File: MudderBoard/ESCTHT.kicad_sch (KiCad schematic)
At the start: 4 parts, among them U4 LM5122QMH/NOPB

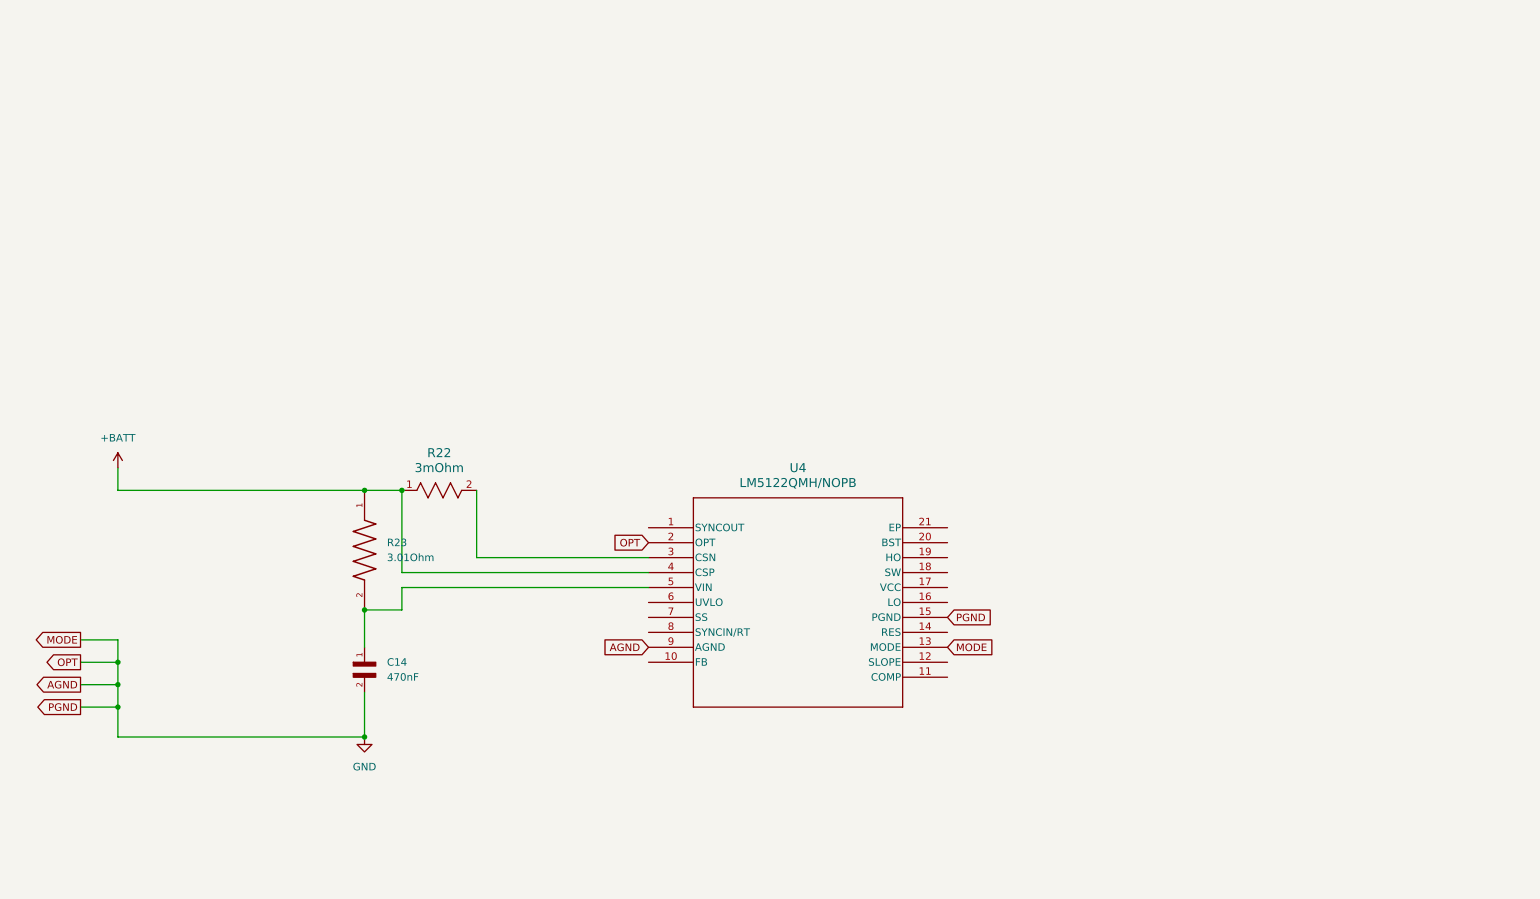
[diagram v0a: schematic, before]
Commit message: Updating the ESC Controller
Completed design without selecting footprints.
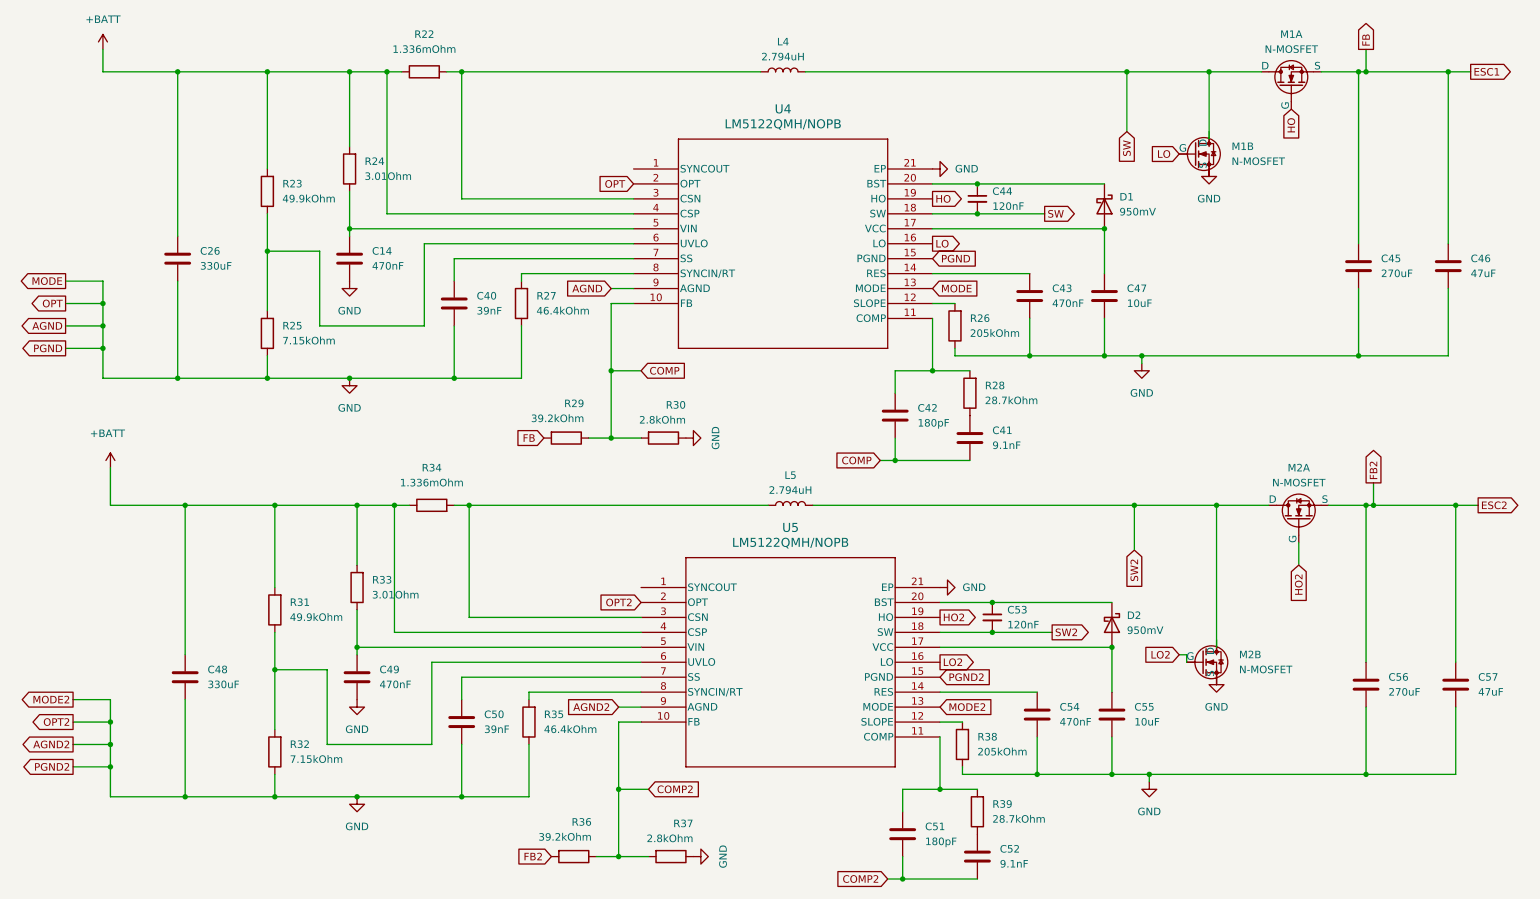
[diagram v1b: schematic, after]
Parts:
- removed C14: 470nF, GRM188R71E474KA12D:CAPC1608X90N, symbol GRM188R71E474KA12D:GRM188R71E474KA12D
- removed R22: 3mOhm, RES_R1206_ROM, symbol PMR18EZPFV3L00:PMR18EZPFV3L00
- removed R23: 3.01Ohm, CRCW04023R01FKED:RESC1005X40N, symbol CRCW04023R01FKED:CRCW04023R01FKED
- added C14, C43, C49, C54: 470nF, symbol Device:C
- added C26, C48: 330uF, symbol Device:C
- added C40, C50: 39nF, symbol Device:C
- added C41, C52: 9.1nF, symbol Device:C
- added C42, C51: 180pF, symbol Device:C
- added C44, C53: 120nF, symbol Device:C_Small
- added C45, C56: 270uF, symbol Device:C
- added C46, C57: 47uF, symbol Device:C
- added C47, C55: 10uF, symbol Device:C
- added D1, D2: 950mV, symbol Device:D_Schottky
- added L4, L5: 2.794uH, symbol Device:L
- added M1, M2: N-MOSFET, symbol DI110N04PQ-AQ:nMOS
- added R22, R34: 1.336mOhm, symbol Device:R
- added R23, R31: 49.9kOhm, symbol Device:R
- added R24, R33: 3.01Ohm, symbol Device:R
- added R25, R32: 7.15kOhm, symbol Device:R
- added R26, R38: 205kOhm, symbol Device:R
- added R27, R35: 46.4kOhm, symbol Device:R
- added R28, R39: 28.7kOhm, symbol Device:R
- added R29, R36: 39.2kOhm, symbol Device:R
- added R30, R37: 2.8kOhm, symbol Device:R
- added U5: LM5122QMH/NOPB, HTSSOP20, symbol 2024-05-03_20-03-19:LM5122QMH_NOPB
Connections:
- net +BATT: now also C26.1, C48.1, R22.1, R23.2, R24.2, R31.2, R33.2, R34.1, U5.4 (CSP)
- net GND: now also U4.21 (EP), C14.2, C26.2, C40.2, C43.2, C45.2, C46.2, C47.2, C48.2, C49.2, C50.2, C54.2, C55.2, C56.2, C57.2, M1.3 (S), M2.3 (S), R25.1, R26.1, R27.1, R30.1, R32.1, R35.1, R37.1, R38.1, U5.13 (MODE), U5.15 (PGND), U5.2 (OPT), U5.21 (EP), U5.9 (AGND)
- net at U4.5 (VIN): now also C14.1, R24.1
- net COMP: now reaches U4.10 (FB)
- net COMP: now also C41.2, C42.2, R29.1, R30.2
- net at U4.11 (COMP): now also C42.1, R28.2
- net at U4.12 (SLOPE): now also R26.2
- net at U4.14 (RES): now also C43.1
- net LO: now reaches U4.16 (LO)
- net LO: now also M1.4 (G)
- net at U4.17 (VCC): now also C47.1, D1.2 (A)
- net SW: now reaches U4.18 (SW)
- net SW: now also C44.2, L4.2, M1.3 (D), M1.5 (D)
- net HO: now reaches U4.19 (HO)
- net HO: now also M1.1 (G)
- net at U4.20 (BST): now also C44.1, D1.1 (K)
- net at U4.3 (CSN): now also L4.1, R22.2
- net at U4.6 (UVLO): now also R23.1, R25.2
- net at U4.7 (SS): now also C40.1
- net at U4.8 (SYNCIN/RT): now also R27.2
- new net: R31.1, R32.2, U5.6 (UVLO)
- new net: L5.1, R34.2, U5.3 (CSN)
- new net: C54.1, U5.14 (RES)
- new net: C41.1, R28.1
- new net: C52.1, R39.1
- new net: C50.1, U5.7 (SS)
- new net: C51.1, R39.2, U5.11 (COMP)
- new net: R38.2, U5.12 (SLOPE)
- new net: C55.1, D2.2 (A), U5.17 (VCC)
- new net: C53.1, D2.1 (K), U5.20 (BST)
- new net: C49.1, R33.1, U5.5 (VIN)
- new net: R35.2, U5.8 (SYNCIN/RT)
- new net COMP2: C51.2, C52.2, R36.1, R37.2, U5.10 (FB)
- new net ESC1: C45.1, C46.1, M1.2 (S), R29.2
- new net ESC2: C56.1, C57.1, M2.2 (S), R36.2
- new net HO2: M2.1 (G), U5.19 (HO)
- new net LO2: M2.4 (G), U5.16 (LO)
- new net SW2: C53.2, L5.2, M2.3 (D), M2.5 (D), U5.18 (SW)
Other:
- moved on the sheet: U4

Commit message: ESC Boost Controllers
Added test points and status LEDs.
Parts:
- added D4, D5: LED, LED_SMD:LED_0201_0603Metric, symbol Device:LED
- added R49, R50: 680, symbol Device:R
- added TP1, TP10, TP11, TP12, TP13, TP14, TP15, TP16, TP17, TP18, TP19, TP2, TP20, TP21, TP22, TP23, TP24, TP25, TP26, TP27, TP28, TP29, TP3, TP30, TP31, TP32, TP4, TP5, TP6, TP7, TP8, TP9: TestPoint, TestPoint:TestPoint_Keystone_5000-5004_Miniature, symbol Connector:TestPoint
- C26, C48: value 330uF -> 180uF
- C41, C52: value 9.1nF -> 4.7nF
- C42, C51: value 180pF -> 100pF
- C44, C53: value 120nF -> 100nF
- L4, L5: value 2.794uH -> 2.352uH
- R22, R34: value 1.336mOhm -> 1.5mOhm
- R25, R32: value 7.15kOhm -> 6.49kOhm
- R26: value 205kOhm -> 165kOhm
- R27, R35: value 46.4kOhm -> 38.3kOhm
- R28, R39: value 28.7kOhm -> 44.2kOhm
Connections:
- net +BATT: now also TP1.1, TP15.1
- net COMP: now also TP12.1
- net COMP2: now also TP25.1
- net ESC1: now also R49.1, TP4.1
- net ESC2: now also R50.1, TP18.1
- net GND: now also D4.1 (K), D5.1 (K)
- net HO2: now also TP19.1
- net LO: now also TP7.1
- net LO2: now also TP20.1
- net SW: now also TP3.1
- net SW2: now also TP17.1
- net at R31.1, R32.2, U5.6 (UVLO): now also TP32.1
- net at L5.1, R34.2, U5.3 (CSN): now also TP16.1
- net at C54.1, U5.14 (RES): now also TP23.1
- net at L4.1, R22.2, U4.3 (CSN): now also TP2.1
- net at R23.1, R25.2, U4.6 (UVLO): now also TP14.1
- net at C14.1, R24.1, U4.5 (VIN): now also TP30.1
- net at C50.1, U5.7 (SS): now also TP27.1
- net at C51.1, R39.2, U5.11 (COMP): now also TP24.1
- net at R38.2, U5.12 (SLOPE): now also TP28.1
- net at C55.1, D2.2 (A), U5.17 (VCC): now also TP22.1
- net at C53.1, D2.1 (K), U5.20 (BST): now also TP21.1
- net at C49.1, R33.1, U5.5 (VIN): now also TP31.1
- net at R35.2, U5.8 (SYNCIN/RT): now also TP26.1
- net at C42.1, R28.2, U4.11 (COMP): now also TP11.1
- net at C40.1, U4.7 (SS): now also TP29.1
- net at C44.1, D1.1 (K), U4.20 (BST): now also TP5.1
- net at C47.1, D1.2 (A), U4.17 (VCC): now also TP6.1
- net at C43.1, U4.14 (RES): now also TP9.1
- net at R27.2, U4.8 (SYNCIN/RT): now also TP13.1
- net at R26.2, U4.12 (SLOPE): now also TP10.1
- new net: D4.2 (A), R50.2
- new net: D5.2 (A), R49.2
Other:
- moved on the sheet: C45, C46, C56, M2B, R23, R24, R31

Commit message: ESC Footprints
Added footprints for ESC controllers. Need to add inductor and fix MOSFETS.
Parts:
- C14, C49: footprint (none) -> Lidar_Foot:CAPC1608X90N
- C26, C48: footprint (none) -> Lidar_Foot:CAP_25SVPF180M
- C40, C50: footprint (none) -> Lidar_Foot:CAPC1005X55N
- C41, C52: footprint (none) -> Lidar_Foot:CAPC2012X75N
- C42, C47, C51, C55: footprint (none) -> Lidar_Foot:CAPC2012X135N
- C43, C54: footprint (none) -> Lidar_Foot:CAPC2012X95N
- C45, C56: footprint (none) -> Lidar_Foot:CAP_EEHZA1V271P
- C46, C57: footprint (none) -> Lidar_Foot:CAPC3216X180N
- D1, D2: footprint (none) -> Lidar_Foot:CR_DO-214ACSMA_TWS
- D4, D5: footprint LED_SMD:LED_0201_0603Metric -> Lidar_Foot:LED_DRD1204W-TR
- M1, M2: footprint (none) -> Lidar_Foot:TRANS_CSD17308Q3
- R22, R34: footprint (none) -> Lidar_Foot:RESC6432X110N
- R23, R24, R25, R26, R27, R30, R31, R32, R33, R35, R37, R38: footprint (none) -> Lidar_Foot:RESC1005X40N
- R28, R39: footprint (none) -> Lidar_Foot:RESC0603X28N
- R29, R36: footprint (none) -> Lidar_Foot:RESC1005X35N
- R49, R50: footprint (none) -> Lidar_Foot:RESC3216X70N
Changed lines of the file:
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@@
 			)
 		)
-		(property "Footprint" ""
+		(property "Footprint" "Lidar_Foot:RESC1005X40N"
 			(at 61.468 142.24 90)
 			(effects
@@
 			)
 		)
-		(property "Footprint" ""
+		(property "Footprint" "Lidar_Foot:RESC1005X40N"
 			(at 127 158.242 90)
 			(effects
@@
 			)
 		)
-		(property "Footprint" "LED_SMD:LED_0201_0603Metric"
+		(property "Footprint" "Lidar_Foot:LED_DRD1204W-TR"
 			(at 251.46 128.27 0)
 			(effects
@@
 			)
 		)
-		(property "Footprint" ""
+		(property "Footprint" "Lidar_Foot:CAP_EEHZA1V271P"
 			(at 240.9952 133.35 0)
 			(effects
@@
 			)
 		)
-		(property "Footprint" ""
+		(property "Footprint" "Lidar_Foot:RESC6432X110N"
 			(at 86.36 102.108 90)
 			(effects
@@
 			)
 		)
-		(property "Footprint" ""
+		(property "Footprint" "Lidar_Foot:CAPC2012X95N"
 			(at 190.1952 139.7 0)
 			(effects
@@
 			)
 		)
-		(property "Footprint" ""
+		(property "Footprint" "Lidar_Foot:RESC6432X110N"
 			(at 85.09 28.448 90)
 			(effects
@@
 			)
 		)
-		(property "Footprint" ""
+		(property "Footprint" "Lidar_Foot:RESC1005X40N"
 			(at 60.198 71.12 90)
 			(effects
@@
 			)
 		)
-		(property "Footprint" ""
+		(property "Footprint" "Lidar_Foot:CAPC2012X75N"
 			(at 178.7652 92.71 0)
 			(effects
@@
 			)
 		)
-		(property "Footprint" ""
+		(property "Footprint" "Lidar_Foot:CAPC2012X75N"
 			(at 180.0352 163.83 0)
 			(effects
@@
 			)
 		)
-		(property "Footprint" ""
+		(property "Footprint" "Lidar_Foot:TRANS_CSD17308Q3"
 			(at 237.236 81.788 0)
 			(effects
@@
 			)
 		)
-		(property "Footprint" ""
+		(property "Footprint" "Lidar_Foot:RESC1005X40N"
 			(at 74.168 41.91 90)
 			(effects
@@
 			)
 		)
-		(property "Footprint" ""
+		(property "Footprint" "Lidar_Foot:CAPC1005X55N"
 			(at 92.4052 140.97 0)
 			(effects
@@
 			)
 		)
-		(property "Footprint" ""
+		(property "Footprint" "Lidar_Foot:CAPC2012X135N"
 			(at 167.3352 160.02 0)
 			(effects
@@
 			)
 		)
-		(property "Footprint" ""
+		(property "Footprint" "Lidar_Foot:CAPC2012X135N"
 			(at 166.0652 88.9 0)
 			(effects
@@
 			)
 		)
-		(property "Footprint" ""
+		(property "Footprint" "Lidar_Foot:CAPC1005X55N"
 			(at 91.1352 69.85 0)
 			(effects
@@
 			)
 		)
-		(property "Footprint" ""
+		(property "Footprint" "Lidar_Foot:CR_DO-214ACSMA_TWS"
 			(at 200.66 49.53 0)
 			(effects
@@
 			)
 		)
-		(property "Footprint" ""
+		(property "Footprint" "Lidar_Foot:CAPC2012X95N"
 			(at 188.9252 68.58 0)
 			(effects
@@
 			)
 		)
-		(property "Footprint" ""
+		(property "Footprint" "Lidar_Foot:TRANS_CSD17308Q3"
 			(at 239.522 121.666 0)
 			(effects
@@
 			)
 		)
-		(property "Footprint" ""
+		(property "Footprint" "Lidar_Foot:CAP_25SVPF180M"
 			(at 45.4152 133.35 0)
 			(effects
@@
 			)
 		)
-		(property "Footprint" ""
+		(property "Footprint" "Lidar_Foot:RESC0603X28N"
 			(at 180.848 152.4 90)
 			(effects
@@
 			)
 		)
-		(property "Footprint" ""
+		(property "Footprint" "Lidar_Foot:CAP_25SVPF180M"
 			(at 44.1452 62.23 0)
 			(effects
@@
 					(size 1.27 1.27)
 				)
-				(hide yes)
 			)
 		)
@@
 			)
 		)
-		(property "Footprint" ""
+		(property "Footprint" "Lidar_Foot:TRANS_CSD17308Q3"
 			(at 236.982 44.196 0)
 			(effects
@@
 			)
 		)
-		(property "Footprint" ""
+		(property "Footprint" "Lidar_Foot:RESC1005X40N"
 			(at 103.378 66.04 90)
 			(effects
@@
 			)
 		)
-		(property "Footprint" ""
+		(property "Footprint" "Lidar_Foot:RESC1005X40N"
 			(at 125.73 87.122 90)
 			(effects
@@
 			)
 		)
-		(property "Footprint" ""
+		(property "Footprint" "Lidar_Foot:CAPC1608X90N"
 			(at 73.3552 62.23 0)
 			(effects
@@
 			)
 		)
-		(property "Footprint" ""
+		(property "Footprint" "Lidar_Foot:RESC3216X70N"
 			(at 249.682 115.57 90)
 			(effects
@@
 			)
 		)
-		(property "Footprint" ""
+		(property "Footprint" "Lidar_Foot:CAPC2012X135N"
 			(at 201.6252 68.58 0)
 			(effects
@@
 			)
 		)
-		(property "Footprint" ""
+		(property "Footprint" "Lidar_Foot:CR_DO-214ACSMA_TWS"
 			(at 201.93 120.65 0)
 			(effects
@@
 			)
 		)
-		(property "Footprint" ""
+		(property "Footprint" "Lidar_Foot:RESC1005X40N"
 			(at 75.438 114.3 90)
 			(effects
@@
 			)
 		)
-		(property "Footprint" ""
+		(property "Footprint" "Lidar_Foot:CAPC2012X135N"
 			(at 202.8952 139.7 0)
 			(effects
@@
 			)
 		)
-		(property "Footprint" ""
+		(property "Footprint" "Lidar_Foot:CAPC3216X180N"
 			(at 261.3152 134.62 0)
 			(effects
@@
 			)
 		)
-		(property "Footprint" "LED_SMD:LED_0201_0603Metric"
+		(property "Footprint" "Lidar_Foot:LED_DRD1204W-TR"
 			(at 248.92 54.61 0)
 			(effects
@@
 			)
 		)
-		(property "Footprint" ""
+		(property "Footprint" "Lidar_Foot:RESC1005X40N"
 			(at 177.038 69.85 90)
 			(effects
@@
 			)
 		)
-		(property "Footprint" ""
+		(property "Footprint" "Lidar_Foot:RESC1005X40N"
 			(at 61.468 113.03 90)
 			(effects
@@
 			)
 		)
-		(property "Footprint" ""
+		(property "Footprint" "Lidar_Foot:RESC1005X35N"
 			(at 109.22 87.122 90)
 			(effects
@@
 			)
 		)
-		(property "Footprint" ""
+		(property "Footprint" "Lidar_Foot:RESC1005X35N"
 			(at 110.49 158.242 90)
 			(effects
@@
 			)
 		)
-		(property "Footprint" ""
+		(property "Footprint" "Lidar_Foot:CAPC3216X180N"
 			(at 261.3152 59.69 0)
 			(effects
@@
 			)
 		)
-		(property "Footprint" ""
+		(property "Footprint" "Lidar_Foot:CAP_EEHZA1V271P"
 			(at 238.4552 59.69 0)
 			(effects
@@
 			)
 		)
-		(property "Footprint" ""
+		(property "Footprint" "Lidar_Foot:RESC1005X40N"
 			(at 60.198 41.91 90)
 			(effects
@@
 			)
 		)
-		(property "Footprint" ""
+		(property "Footprint" "Lidar_Foot:TRANS_CSD17308Q3"
 			(at 235.966 8.128 0)
 			(effects
@@
 			)
 		)
-		(property "Footprint" ""
+		(property "Footprint" "Lidar_Foot:RESC1005X40N"
 			(at 104.648 137.16 90)
 			(effects
@@
 			)
 		)
-		(property "Footprint" ""
+		(property "Footprint" "Lidar_Foot:RESC0603X28N"
 			(at 179.578 81.28 90)
 			(effects
@@
 			)
 		)
-		(property "Footprint" ""
+		(property "Footprint" "Lidar_Foot:RESC3216X70N"
 			(at 247.142 40.64 90)
 			(effects
@@
 			)
 		)
-		(property "Footprint" ""
+		(property "Footprint" "Lidar_Foot:RESC1005X40N"
 			(at 178.308 140.97 90)
 			(effects
@@
 			)
 		)
-		(property "Footprint" ""
+		(property "Footprint" "Lidar_Foot:CAPC1608X90N"
 			(at 74.6252 133.35 0)
 			(effects

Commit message: Imported footprints to layout
Colin - Make note of these

C30,C32 are generic 0805 caps
L4,L5 are basic insuctors, will need to change when we figure this situation out!

U8,U9 changed to same boost IC as Lidar - these are the same right?
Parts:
- C30: renamed from C44; footprint (none) -> Footprints:CAP_CC0805_YAG
- C32: renamed from C53; footprint (none) -> Footprints:CAP_CC0805_YAG
- L4, L5: footprint (none) -> Inductor_SMD:L_Neosid_SM-PIC0512H
- U8: renamed from U4; footprint HTSSOP20 -> Lidar_Foot:SOP65P640X110-21N
- U9: renamed from U5; footprint HTSSOP20 -> Lidar_Foot:SOP65P640X110-21N
- renumbered C26 to C21, C48 to C22, C14 to C23, C49 to C24, C40 to C25, C50 to C26, C42 to C27, C51 to C28, C41 to C29, C52 to C31, C43 to C33, C54 to C34, C47 to C35, C55 to C36, C45 to C37, C56 to C38, C46 to C39, C57 to C40, D1 to D5, D2 to D6, D5 to D7, D4 to D8, M1 to M3, M2 to M4, R23 to R24, R31 to R26, R32 to R27, R24 to R28, R33 to R29, R22 to R30, R34 to R31, R27 to R32, R35 to R33, R29 to R34, R36 to R35, R30 to R36, R26 to R38, R38 to R39, R28 to R40, R39 to R41, R49 to R42, R50 to R43, TP26 to TP10, TP2 to TP11, TP16 to TP12, TP12 to TP13, TP25 to TP14, TP11 to TP15, TP24 to TP16, TP10 to TP18, TP3 to TP19, TP14 to TP2, TP28 to TP20, TP9 to TP21, TP5 to TP22, TP21 to TP24, TP6 to TP25, TP22 to TP26, TP7 to TP27, TP20 to TP28, TP8 to TP29, TP32 to TP3, TP19 to TP30, TP4 to TP31, TP18 to TP32, TP15 to TP4, TP30 to TP5, TP31 to TP6, TP29 to TP7, TP27 to TP8, TP13 to TP9
